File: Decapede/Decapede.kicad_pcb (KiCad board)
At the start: 2 copper layers, 142 x 110 mm, 305 parts, among them J1 I2C, J10 FET3, J11 FET4, J12 FET6, J13 FET7, J14 FET8, J15 FET9, J16 Th1, J17 Th2, J18 Th3, J19 Th4, J20 Th5, J21 Th6, J22 Th7, J23 FET5, J24 FET10, J25 GPIO, J27 SDCARD-HOLDER, J28 Th8, J29 Th9, J30 Th10, J8 FET1, J9 FET2, M1 PCB_GREEN_RMC, P1 Power, P10 E_out, P11 MS_E, P12 X_out, P13 MS_X, P14 Y_out, P15 MS_Y, P16 Z_out, P17 MS_Z, P18 W_out, P19 MS_W, P2 MS_A, P20 V_out, P21 MS_V, P22 X_min, P23 X_max, P24 Y_min, P25 Y_max, P26 Z_min, P27 Z_max, P28 W_min, P29 W_max, P3 A_out, P30 V_min, P31 V_max, P32 A_min, P33 A_max, P34 B_min, P35 B_max, P36 C_min, P37 C_max, P38 D_min, P39 D_max, P4 MS_B, P40 E_min, P41 E_max, P42 Serial, P43 Aux, P44 SPI, P5 B_out, P6 C_out, P7 MS_C, P8 D_out, P9 MS_D, Q1 BUK7226-75A,118, Q10 BC807,215, Q11 BC817-25,215, Q12 BC817-25,215, Q13 PSMN023-40YLCX, Q14 PSMN023-40YLCX, Q15 BC807,215, Q16 BC807,215, Q17 BC817-25,215, Q18 BC817-25,215, Q19 PSMN023-40YLCX, Q2 BUK964R8-60E,118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

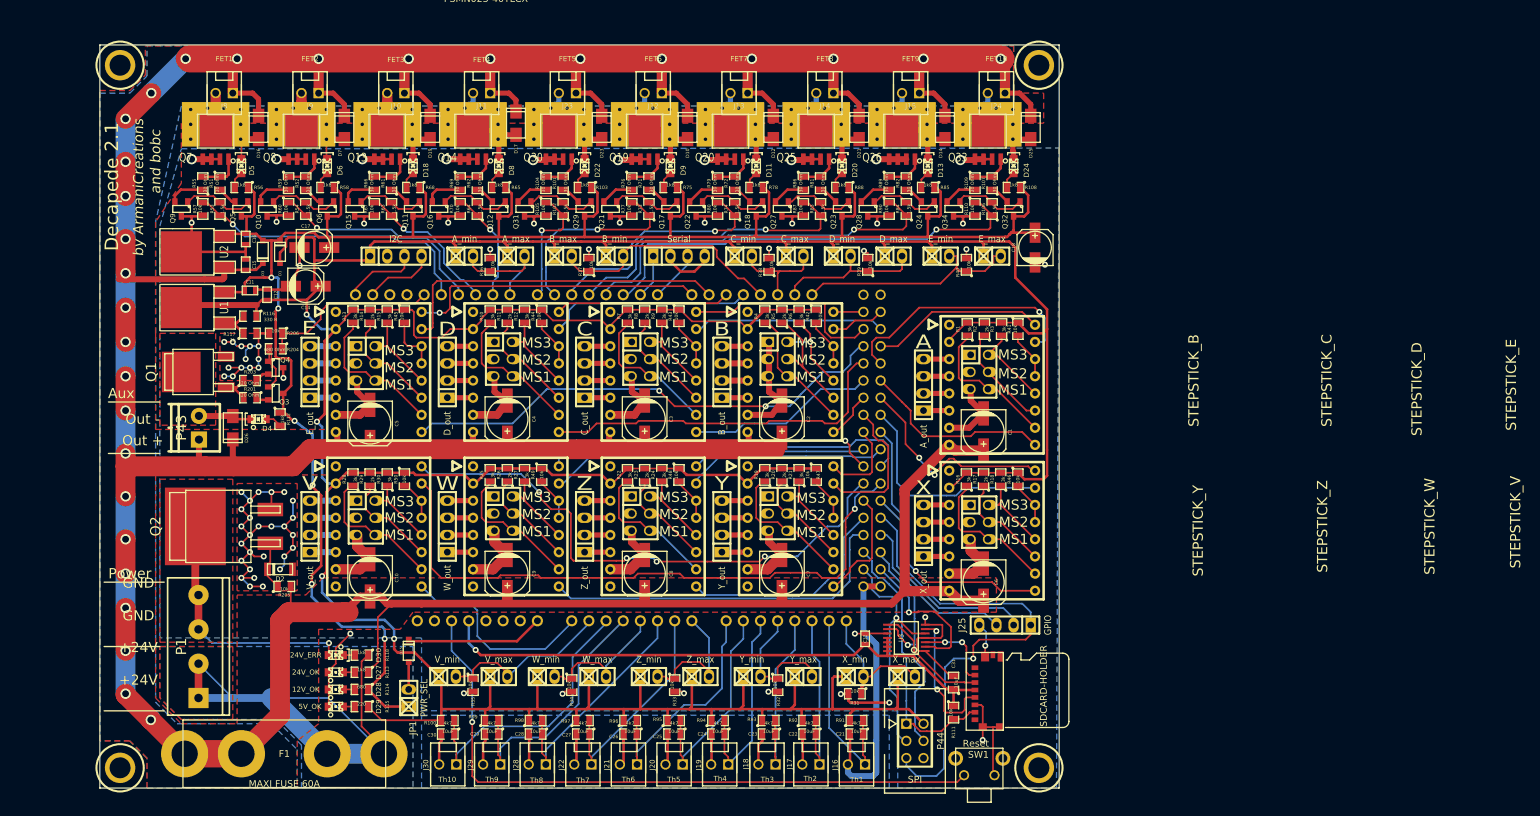
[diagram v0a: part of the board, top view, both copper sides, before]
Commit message: Decapede update: add fuses for each main section; change endstops to use 0V instead of 5V; more space for stepper drivers to allow latching connectors
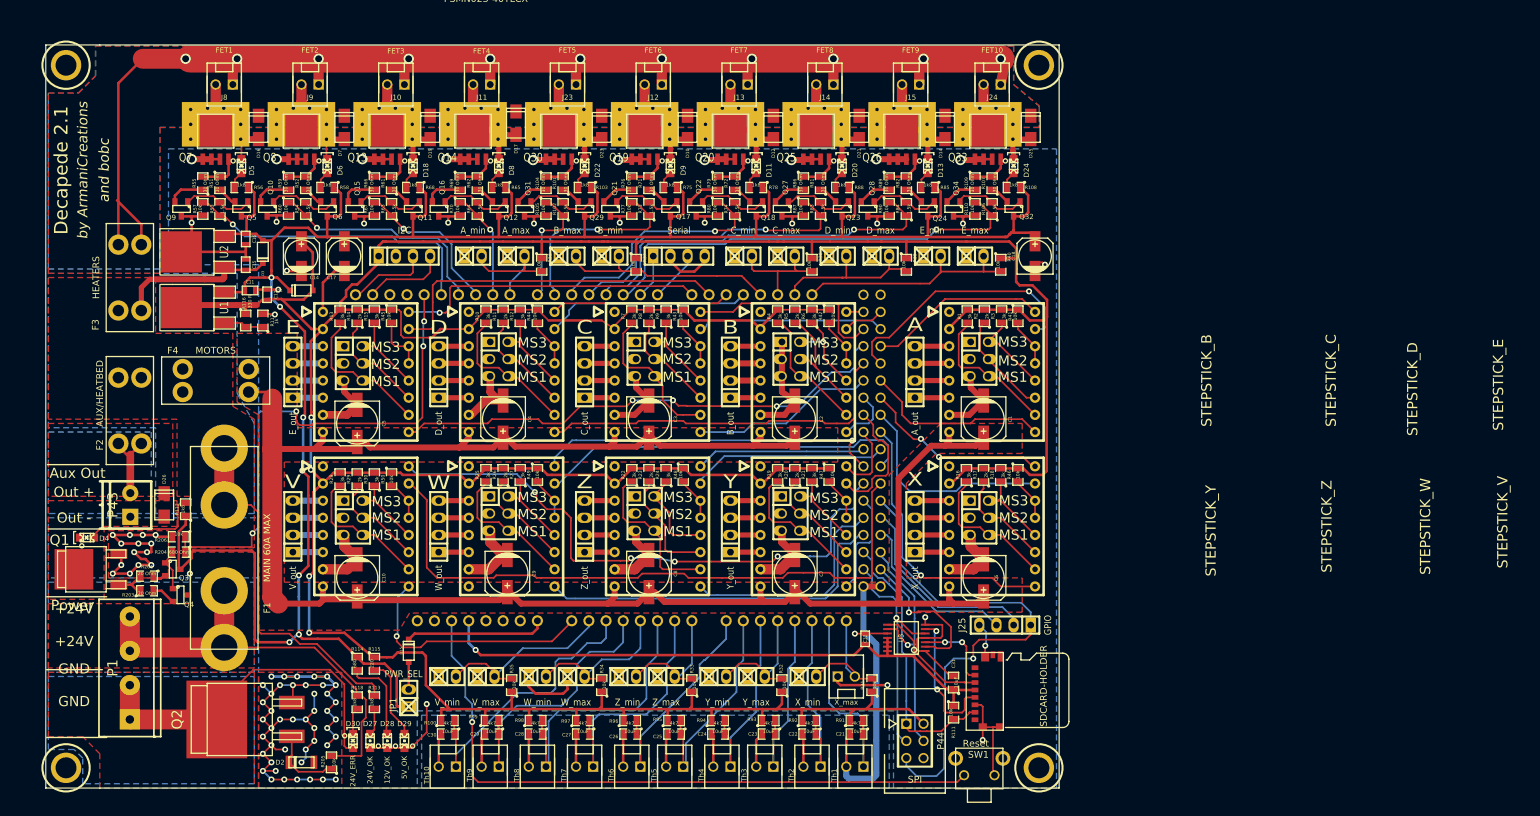
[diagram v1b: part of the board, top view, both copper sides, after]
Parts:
- added F2: AUX/HEATBED, Keystone_3568, F.Cu at (55.2, 96.5)
- added F3: HEATERS, Keystone_3568, F.Cu at (55.2, 76.8)
- added F4: MOTORS, Keystone_3568, F.Cu at (67.9, 92.1)
- F1: value MAXI FUSE 60A -> MAIN 60A MAX
- P23: footprint pin_strip_2 -> CONN_KK_2.54_2W
- P43: value Aux -> Aux Out
- moved Q4 36.5 mm to (62.7, 123.8)
- moved R203 34.6 mm to (57.8, 123.2)
- moved R204 33.3 mm to (62.5, 117.5)
- moved R206 33.3 mm to (62.5, 115.2)
- moved Q1 33.2 mm to (50.2, 120.0)
- moved F1 31.7 mm to (69.2, 116.8), turned to 270 degrees
- moved D4 30.9 mm to (48.9, 115.3)
- moved R201 30.5 mm to (57.8, 121.0)
- moved Q3 30.2 mm to (61.6, 120.0)
- moved D2 28.8 mm to (80.6, 148.6)
- moved Q2 28.8 mm to (73.7, 142.2)
- moved R205 27.0 mm to (85.1, 148.6), turned to 90 degrees
- moved R112 19.3 mm to (63.5, 111.1), turned to 90 degrees
- moved D26 15.3 mm to (60.3, 110.5), turned to 90 degrees
- moved P43 15.3 mm to (54.6, 110.5)
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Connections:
- net +12V renamed +V_GATE
- C1 pad 1: +24V -> +V_MOTOR
- C10 pad 1: +24V -> +V_MOTOR
- C2 pad 1: +24V -> +V_MOTOR
- C3 pad 1: +24V -> +V_MOTOR
- C4 pad 1: +24V -> +V_MOTOR
- C5 pad 1: +24V -> +V_MOTOR
- C6 pad 1: +24V -> +V_MOTOR
- C7 pad 1: +24V -> +V_MOTOR
- C8 pad 1: +24V -> +V_MOTOR
- C9 pad 1: +24V -> +V_MOTOR
- D10 pad 2: +24V -> +V_HEATERS
- D12 pad 2: +24V -> +V_HEATERS
- D14 pad 2: +24V -> +V_HEATERS
- D16 pad 2: +24V -> +V_HEATERS
- D17 pad 2: +24V -> +V_HEATERS
- D19 pad 2: +24V -> +V_HEATERS
- D21 pad 2: +24V -> +V_HEATERS
- D23 pad 2: +24V -> +V_HEATERS
- D25 pad 2: +24V -> +V_HEATERS
- D26 pad 2: +24V -> +V_HEATBED
- D7 pad 2: +24V -> +V_HEATERS
- F1 pad 2: +24V2 -> /Power/24V_IN
- J10 pad 1: +24V -> +V_HEATERS
- J11 pad 1: +24V -> +V_HEATERS
- J12 pad 1: +24V -> +V_HEATERS
- J13 pad 1: +24V -> +V_HEATERS
- J14 pad 1: +24V -> +V_HEATERS
- J15 pad 1: +24V -> +V_HEATERS
- J23 pad 1: +24V -> +V_HEATERS
- J24 pad 1: +24V -> +V_HEATERS
- J8 pad 1: +24V -> +V_HEATERS
- J9 pad 1: +24V -> +V_HEATERS
- P1 pad 1: +24V2 -> /Power/GND_IN
- P1 pad 2: +24V2 -> /Power/GND_IN
- P1 pad 3: /Power/GND_IN -> /Power/24V_IN
- P1 pad 4: /Power/GND_IN -> /Power/24V_IN
- P22 pad 1: +V_LOGIC -> GND
- P23 pad 1: +V_LOGIC -> GND
- P24 pad 1: +V_LOGIC -> GND
- P25 pad 1: +V_LOGIC -> GND
- P26 pad 1: +V_LOGIC -> GND
- P27 pad 1: +V_LOGIC -> GND
- P28 pad 1: +V_LOGIC -> GND
- P29 pad 1: +V_LOGIC -> GND
- P30 pad 1: +V_LOGIC -> GND
- P31 pad 1: +V_LOGIC -> GND
- P32 pad 1: +V_LOGIC -> GND
- P33 pad 1: +V_LOGIC -> GND
- P34 pad 1: +V_LOGIC -> GND
- P35 pad 1: +V_LOGIC -> GND
- P36 pad 1: +V_LOGIC -> GND
- P37 pad 1: +V_LOGIC -> GND
- P38 pad 1: +V_LOGIC -> GND
- P39 pad 1: +V_LOGIC -> GND
- P40 pad 1: +V_LOGIC -> GND
- P41 pad 1: +V_LOGIC -> GND
- P43 pad 1: +24V -> /Power/AUX_RTN
- P43 pad 2: /Power/AUX_RTN -> +V_HEATBED
- R118 pad 1: +24V2 -> /Power/24V_IN
- R205 pad 2: +24V -> /Power/24V_IN
- R31 pad 1: X_axis -> +V_LOGIC
- R31 pad 2: GND -> X_axis
- R32 pad 1: Y_axis -> +V_LOGIC
- R32 pad 2: GND -> Y_axis
- R33 pad 1: Z_axis -> +V_LOGIC
- R33 pad 2: GND -> Z_axis
- R34 pad 1: W_axis -> +V_LOGIC
- R34 pad 2: GND -> W_axis
- R35 pad 1: V_axis -> +V_LOGIC
- R35 pad 2: GND -> V_axis
- R36 pad 1: A_axis -> +V_LOGIC
- R36 pad 2: GND -> A_axis
- R37 pad 1: B_axis -> +V_LOGIC
- R37 pad 2: GND -> B_axis
- R38 pad 1: C_axis -> +V_LOGIC
- R38 pad 2: GND -> C_axis
- R39 pad 1: D_axis -> +V_LOGIC
- R39 pad 2: GND -> D_axis
- R40 pad 1: E_axis -> +V_LOGIC
- R40 pad 2: GND -> E_axis
- StepStick_1 pad 8: +24V -> +V_MOTOR
- StepStick_10 pad 8: +24V -> +V_MOTOR
- StepStick_2 pad 8: +24V -> +V_MOTOR
- StepStick_3 pad 8: +24V -> +V_MOTOR
- StepStick_4 pad 8: +24V -> +V_MOTOR
- StepStick_5 pad 8: +24V -> +V_MOTOR
- StepStick_6 pad 8: +24V -> +V_MOTOR
- StepStick_7 pad 8: +24V -> +V_MOTOR
- StepStick_8 pad 8: +24V -> +V_MOTOR
- StepStick_9 pad 8: +24V -> +V_MOTOR
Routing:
- net +24V: track 809.9 -> 77.9 mm, vias 29 -> 0
- net +V_HEATERS: track 0.00 -> 323.1 mm, vias 0 -> 11
- net +V_MOTOR: track 0.00 -> 284.0 mm
- net +24V2: track 79.7 -> 0.00 mm
- net /Power/24V_IN: track 0.00 -> 65.5 mm
- net GND: track 389.9 -> 449.1 mm, vias 79 -> 90
- net Aux_output: track 26.7 -> 77.4 mm, vias 0 -> 4
- net +V_LOGIC: track 625.7 -> 576.2 mm
- net +V_GATE: track 317.7 -> 357.7 mm, vias 6 -> 7
- net +V_HEATBED: track 0.00 -> 16.6 mm
- net N-000009: track 2.52 -> 17.7 mm
- net /Power/GND_IN: track 37.4 -> 52.4 mm, vias 1 -> 0
- net N-000001: track 1.81 -> 13.2 mm
- net N-000002: track 1.81 -> 12.1 mm
- net TH8: track 34.8 -> 42.0 mm
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- added copper zone on B.Cu, net +V_HEATBED
- added copper zone on F.Cu, net +V_HEATBED
- added copper zone on B.Cu, net +V_HEATERS
- added copper zone on F.Cu, net +V_HEATERS
- added copper zone on F.Cu, net +V_MOTOR
- added copper zone on B.Cu, net /Power/24V_IN
- added copper zone on F.Cu, net /Power/24V_IN
- added copper zone on B.Cu, net /Power/GND_IN
- removed copper zone on B.Cu, net +24V2
- removed copper zone on F.Cu, net +24V2
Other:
- board size 142 x 110 mm -> 150 x 110 mm
